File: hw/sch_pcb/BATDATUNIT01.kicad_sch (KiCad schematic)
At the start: 115 parts, among them IC1 MAX14502AETL+, J1 USBC_USB4105-GF-A, J22 HEADER_2x03, J4 46436-9327, J9 SD_Card-FPS009-4200-0, Q1 BC817-25, Q2 BC817-25, Q3 BC817-25, Q4 BC817-25, SW3 KMT031, SW3 SKRTLAE010, SW4 KMT031, SW4 SKRTLAE010, U10 ATMEGA1284P-AU, U11 PCF85263A, U11 TCA4307, U2 USBLC6-2SC6, U3 FT260Q-T, U4 PCA9541ABS/01, U6 AT24CS64-SSHM, U6 SHT35-DIS, U7 TMUX1574DYYR, Y1 19.2 MHz, Y1 8 MHz, Y2 ABS07-120-32.768KHZ-T

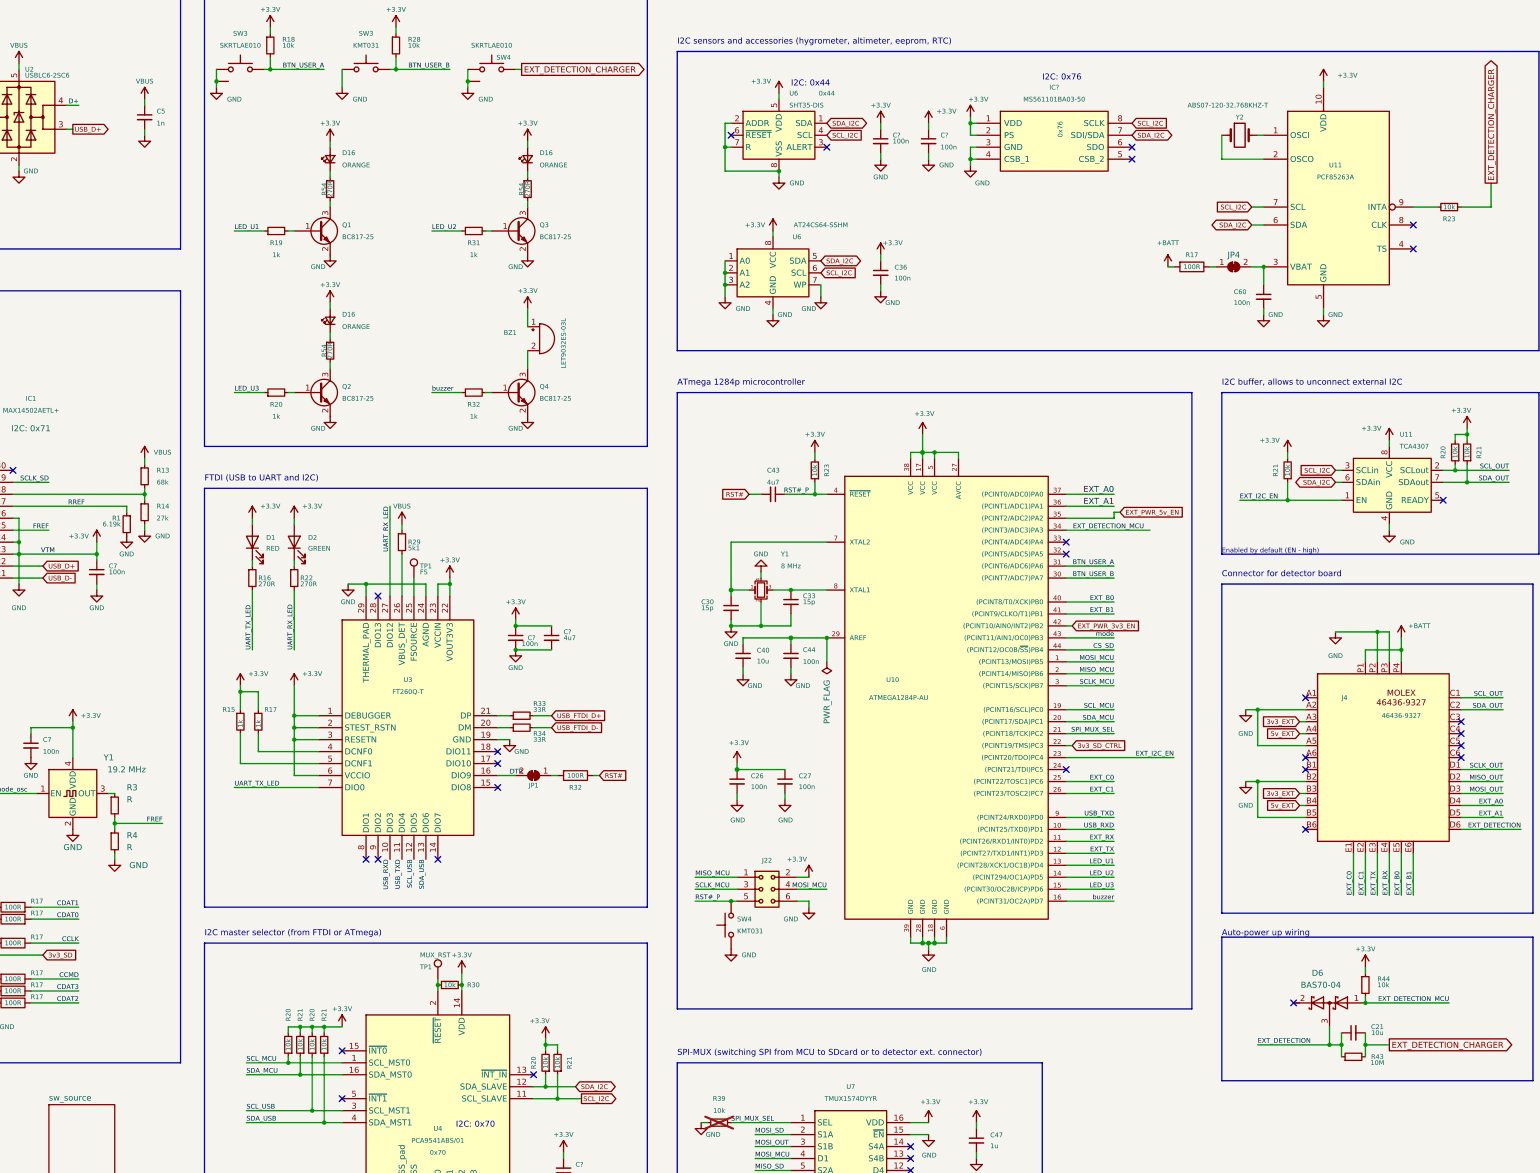
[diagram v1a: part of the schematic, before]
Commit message: Add power consumption notes to schematics.
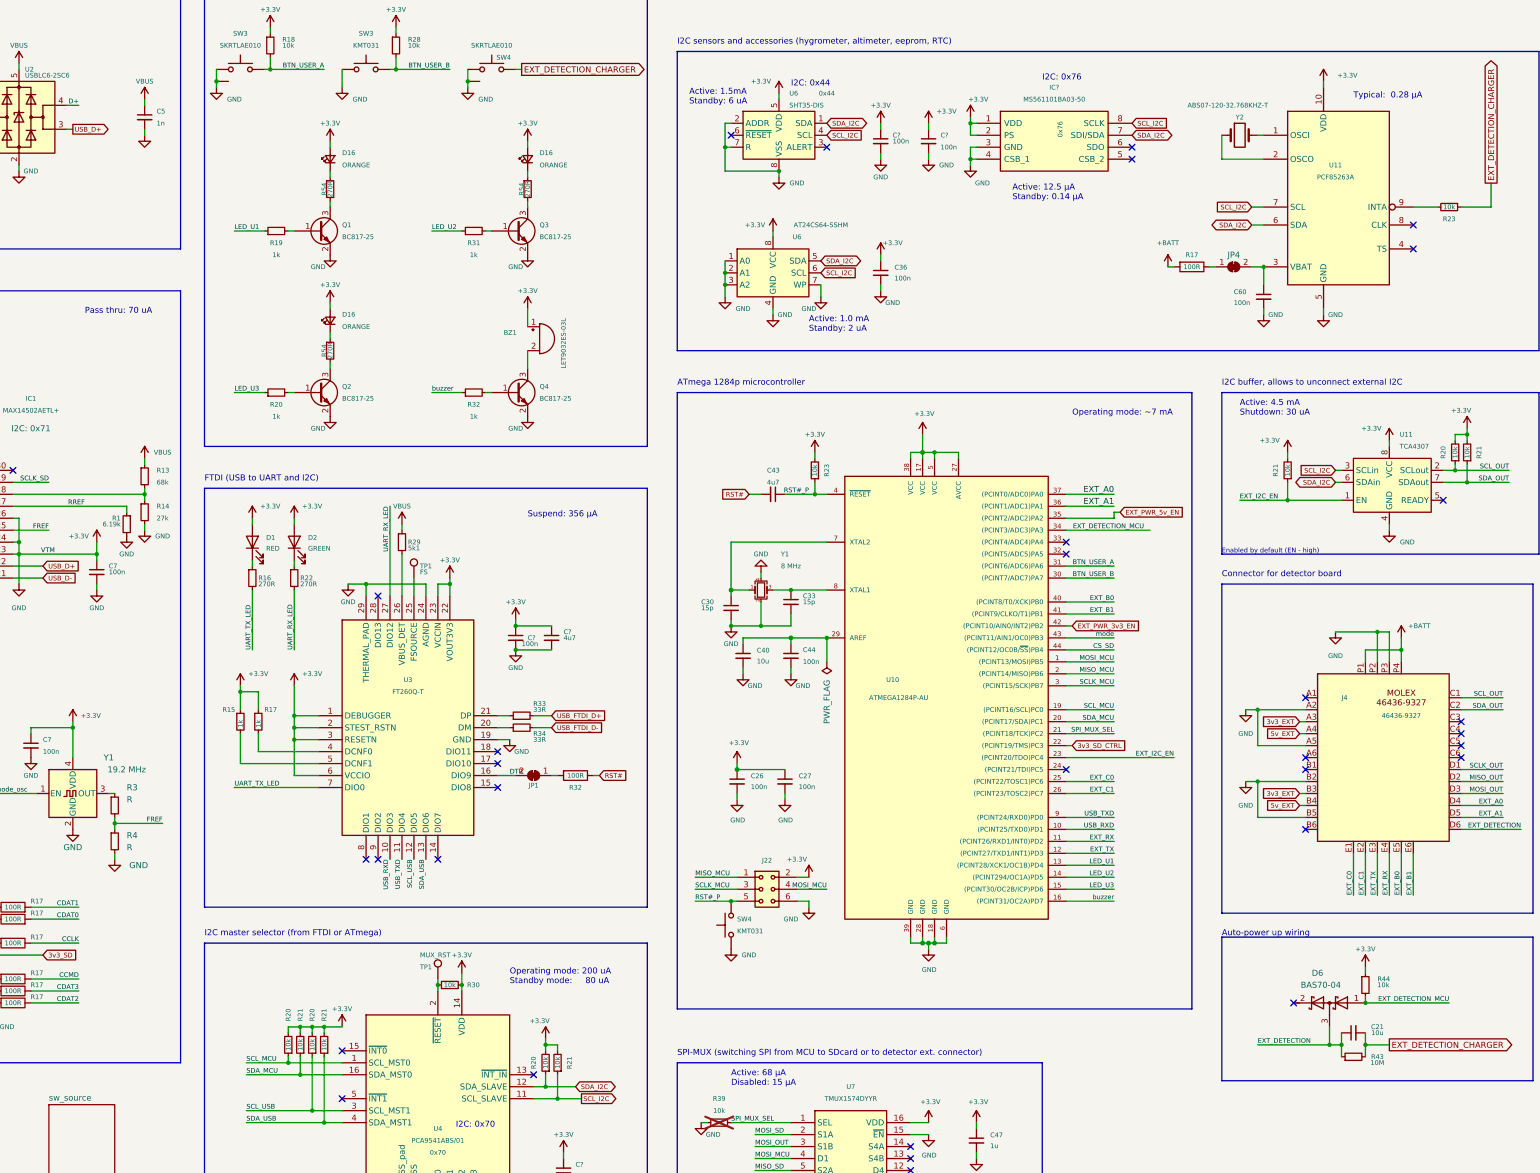
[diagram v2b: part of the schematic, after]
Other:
- note added: "Active: 1.0 mA Standby: 2 uA"
- note added: "Active: 1.5mA Standby: 6 uA"
- note added: "Active: 12.5 μA Standby: 0.14 μA"
- note added: "Active: 4.5 mA Shutdown: 30 uA"
- note added: "Active: 68 μA Disabled: 15 μA"
- note added: "Operating mode: 200 uA Standby mode: 80 uA"
- note added: "Operating mode: ~7 mA"
- note added: "Pass thru: 70 uA"
- note added: "Suspend: 356 μA"
- note added: "Typical: 0.28 μA"
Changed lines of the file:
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@@
     (effects (font (size 1.27 1.27)) (justify left bottom))
   )
+  (text "Active: 4.5 mA\nShutdown: 30 uA" (at 341.63 109.22 0)
+    (effects (font (size 1.27 1.27)) (justify left bottom))
+  )
+  (text "Active: 1.5mA\nStandby: 6 uA" (at 224.79 43.18 0)
+    (effects (font (size 1.27 1.27)) (justify left bottom))
+  )
+  (text "Active: 1.0 mA\nStandby: 2 uA" (at 250.19 91.44 0)
+    (effects (font (size 1.27 1.27)) (justify left bottom))
+  )
+  (text "Suspend: 356 μA" (at 190.5 130.81 0)
+    (effects (font (size 1.27 1.27)) (justify left bottom))
+  )
   (text "FTDI (USB to UART and I2C)" (at 121.92 123.19 0)
     (effects (font (size 1.27 1.27)) (justify left bottom))
@@
     (effects (font (size 1.27 1.27)) (justify left bottom))
   )
+  (text "Active: 12.5 μA\nStandby: 0.14 μA" (at 293.37 63.5 0)
+    (effects (font (size 1.27 1.27)) (justify left bottom))
+  )
   (text "Mechanical" (at 15.24 250.19 0)
     (effects (font (size 1.27 1.27)) (justify left bottom))
@@
     (effects (font (size 1.27 1.27)) (justify left bottom))
   )
+  (text "Pass thru: 70 uA" (at 96.52 87.63 0)
+    (effects (font (size 1.27 1.27)) (justify left bottom))
+  )
   (text "USB-C connector and ESD protection" (at 15.24 19.05 0)
     (effects (font (size 1.27 1.27)) (justify left bottom))
   )
+  (text "Typical:  0.28 μA " (at 365.76 41.91 0)
+    (effects (font (size 1.27 1.27)) (justify left bottom))
+  )
   (text "I2C sensors and accessories (hygrometer, altimeter, eeprom, RTC)"
     (at 222.25 30.48 0)
@@
     (effects (font (size 1.27 1.27)) (justify left bottom))
   )
+  (text "Operating mode: ~7 mA" (at 306.07 109.22 0)
+    (effects (font (size 1.27 1.27)) (justify left bottom))
+  )
   (text "Auto-power up wiring" (at 337.82 219.71 0)
     (effects (font (size 1.27 1.27)) (justify left bottom))
   )
+  (text "Active: 68 μA\nDisabled: 15 μA" (at 233.68 251.46 0)
+    (effects (font (size 1.27 1.27)) (justify left bottom))
+  )
   (text "Connector for detector board" (at 337.82 143.51 0)
     (effects (font (size 1.27 1.27)) (justify left bottom))
@@
     (effects (font (size 1.27 1.27)) (justify left bottom))
   )
+  (text "Operating mode: 200 uA\nStandby mode: 	80 uA" (at 186.69 229.87 0)
+    (effects (font (size 1.27 1.27)) (justify left bottom))
+  )
   (text "SD card interface (USB to SDcard reader and USB-bridge to FTDI)"
     (at 15.24 81.28 0)
@@
       (effects (font (size 1 1)) (justify left) hide)
     )
-    (property "Datasheet" "http://www.te.com/usa-en/search.html?q=ms5611&source=header" (at 314.96 46.99 0)
+    (property "Datasheet" "https://www.te.com/usa-en/product-MS561101BA03-50.datasheet.pdf" (at 314.96 46.99 0)
       (effects (font (size 1 1)) (justify left) hide)
     )

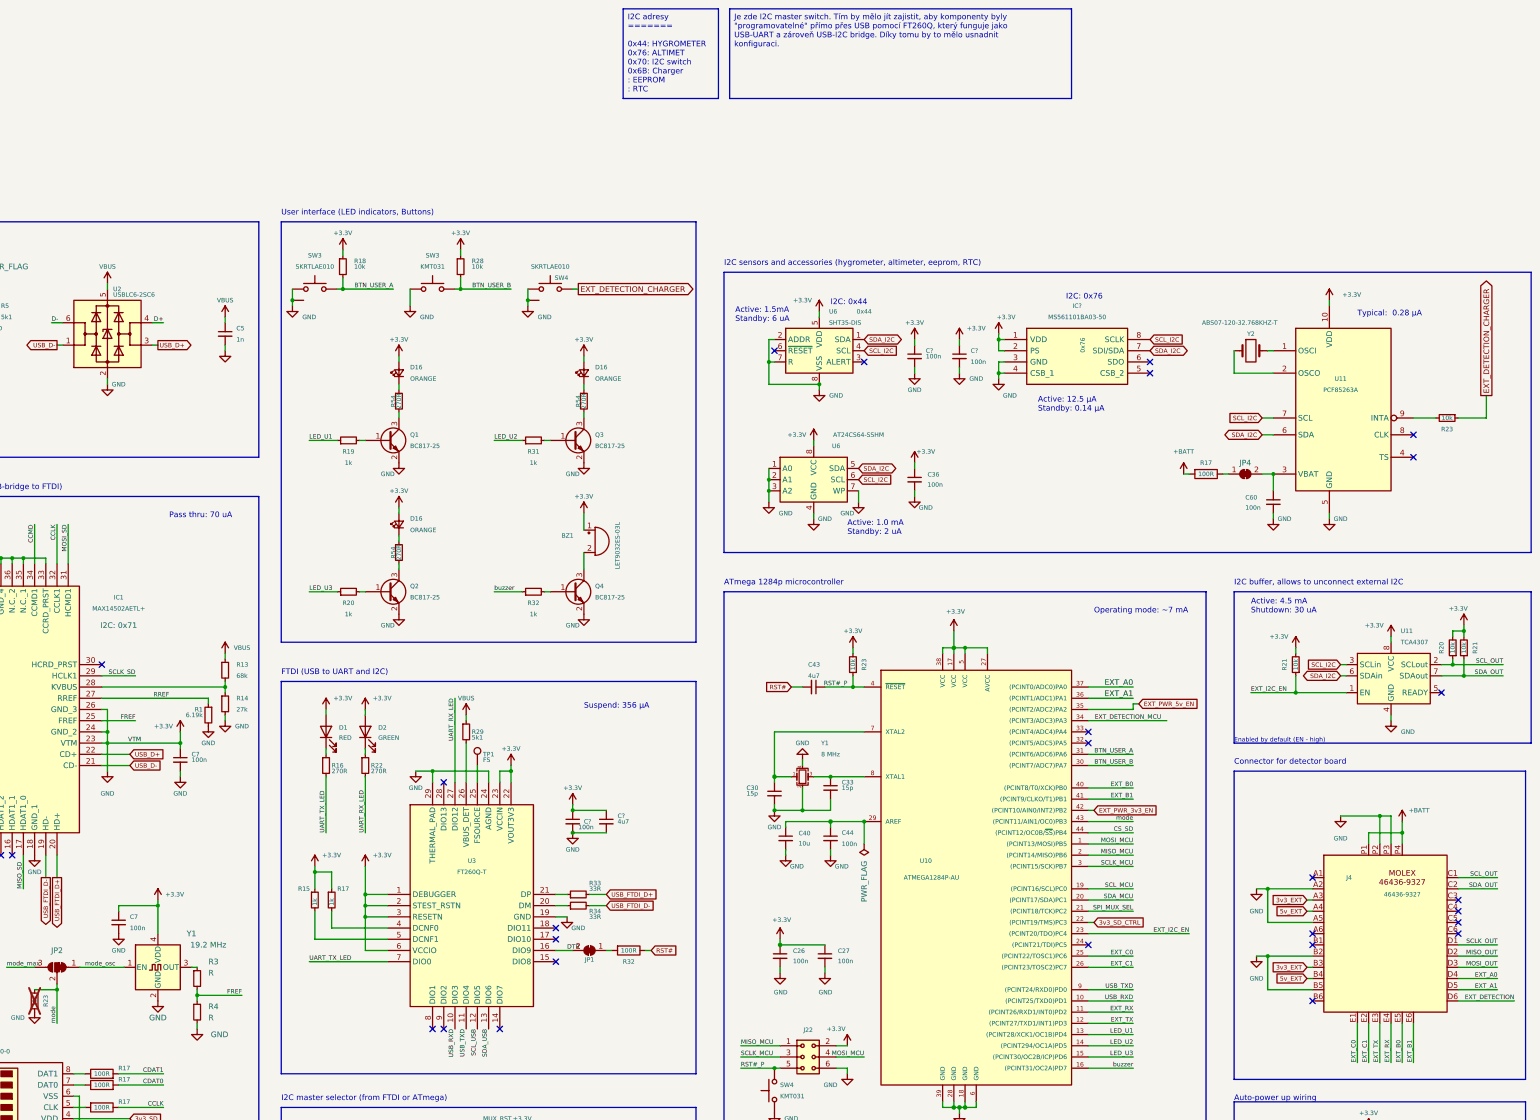
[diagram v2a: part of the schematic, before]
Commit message: Vylepseni, upravy layoutu, zmena ovladani ledky, reset pin do molex konektoru
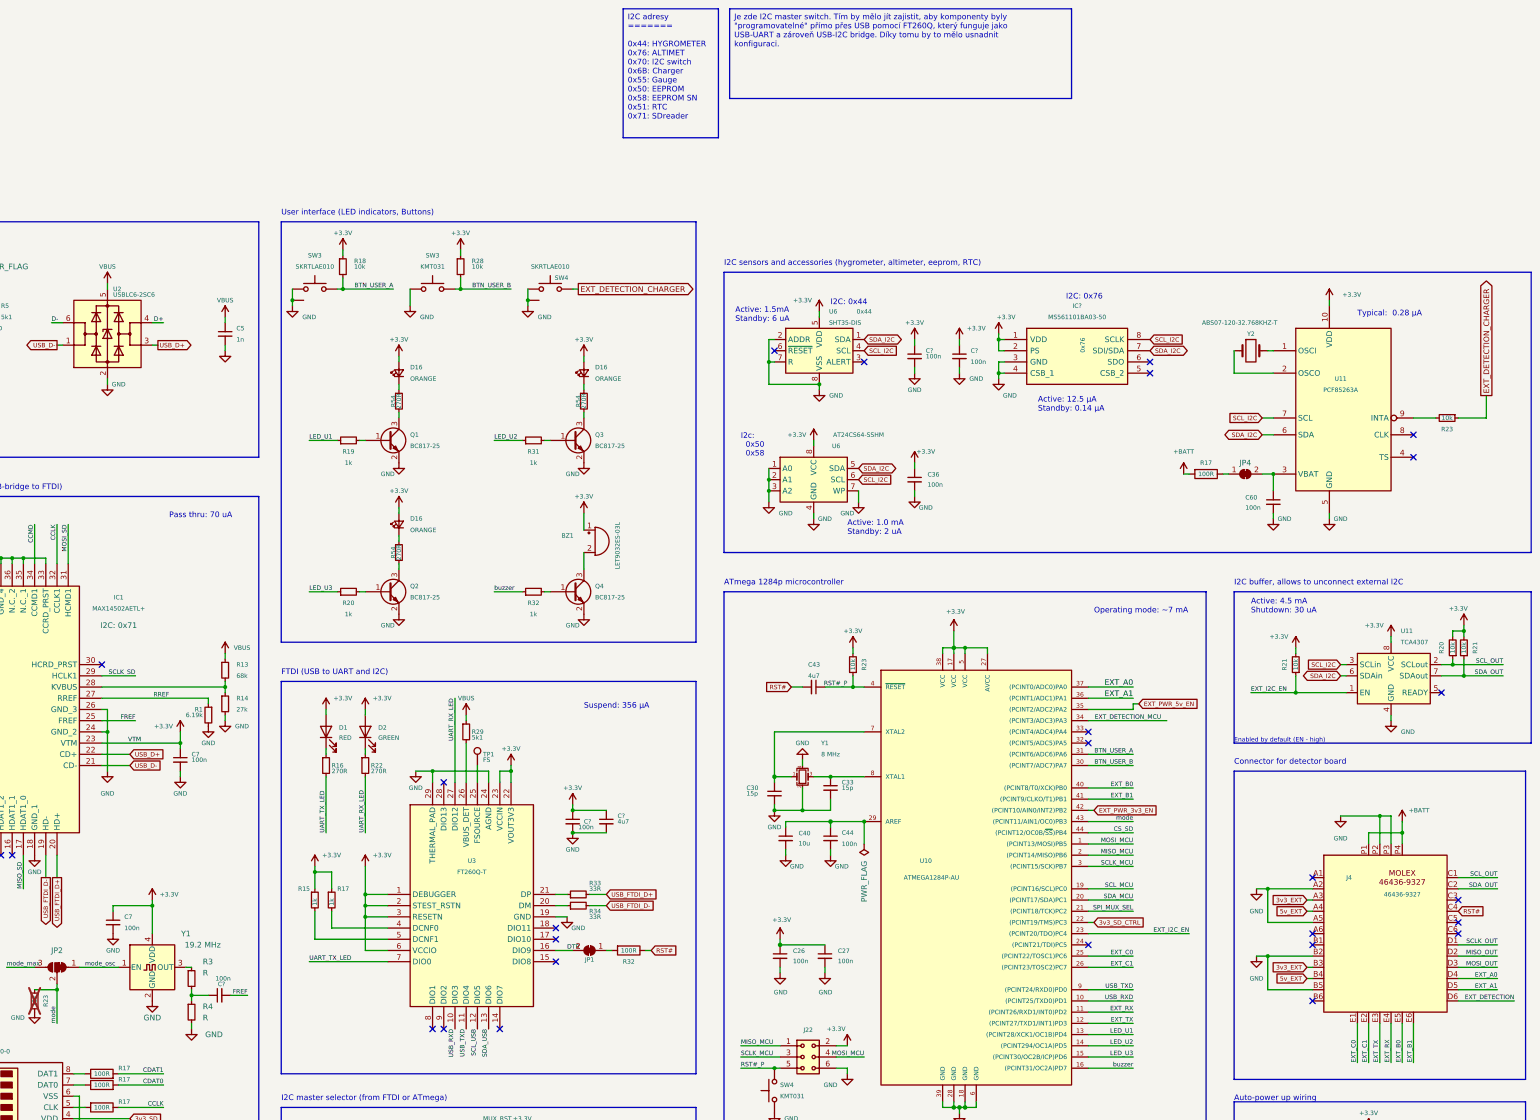
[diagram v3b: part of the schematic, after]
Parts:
- added C?: 100n, Capacitor_SMD:C_0805_2012Metric, symbol Device:C_Small
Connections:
- net +3.3V: no longer C26.2, C27.2, C30.2, C33.2, C36.2, C40.2, C44.2, C47.2, C5.2, C5.2, C6.2, C60.2, C7.2, C7.2, C?.2, C?.2, C?.2, C?.2, C?.2, H1.1, H2.1, H3.1, H4.1, IC1.18 (GND_1), IC1.24 (GND_2), IC1.26 (GND_3), IC1.33 (CCRD_PRST), IC1.35 (N.C._1), IC1.36 (N.C._2), IC1.37 (GND_4), IC1.41 (GND_5), IC?.3 (GND), IC?.4 (CSB_1), J1.A1/B12 (GND), J1.B1/A12 (GND), J1.G1 (SHIELD), J1.G2 (SHIELD), J1.G3 (SHIELD), J1.G4 (SHIELD), J22.6, J4.A2, J4.A5, J4.B2, J4.B5, J4.P2, J4.P3, J9.12 (SHELL1), J9.3 (VSS), J9.6 (VSS), JP1.3 (B), Q1.2 (E), Q2.2 (E), Q3.2 (E), Q4.2 (E), R1.2, R14.2, R2.1, R23.1, R39.1, R4.2, R5.1, SW3.2, SW3.2, SW3.GND (SHIELD), SW4.1, SW4.2, SW4.GND (SHIELD), U10.18 (GND), U10.28 (GND), U10.39 (GND), U10.6 (GND), U11.4 (GND), U11.5 (GND), U2.2 (GND), U3.19 (GND), U3.24 (AGND), U3.29 (THERMAL_PAD), U4.10 (A3), U4.17 (VSS_pad), U4.6 (VSS), U4.7 (A0), U4.8 (A1), U4.9 (A2), U6.1 (A0), U6.2 (A1), U6.2 (ADDR), U6.3 (A2), U6.4 (GND), U6.7 (R), U6.7 (WP), U6.8 (VSS), U6.9 (VSS), U7.15 (~{EN}), U7.8 (GND), Y1.2, Y1.2 (GND), Y1.4
- net FREF: now also C?.2; no longer R3.2, R4.1
- net RST#: now also J4.C4
- new net: C?.1, R3.2, R4.1
- new net GND: C26.2, C27.2, C30.2, C33.2, C36.2, C40.2, C44.2, C47.2, C5.2, C5.2, C6.2, C60.2, C7.2, C7.2, C?.2, C?.2, C?.2, C?.2, C?.2, H1.1, H2.1, H3.1, H4.1, IC1.18 (GND_1), IC1.24 (GND_2), IC1.26 (GND_3), IC1.33 (CCRD_PRST), IC1.35 (N.C._1), IC1.36 (N.C._2), IC1.37 (GND_4), IC1.41 (GND_5), IC?.3 (GND), IC?.4 (CSB_1), J1.A1/B12 (GND), J1.B1/A12 (GND), J1.G1 (SHIELD), J1.G2 (SHIELD), J1.G3 (SHIELD), J1.G4 (SHIELD), J22.6, J4.A2, J4.A5, J4.B2, J4.B5, J4.P2, J4.P3, J9.12 (SHELL1), J9.3 (VSS), J9.6 (VSS), JP1.3 (B), Q1.2 (E), Q2.2 (E), Q3.2 (E), Q4.2 (E), R1.2, R14.2, R2.1, R23.1, R39.1, R4.2, R5.1, SW3.2, SW3.2, SW3.GND (SHIELD), SW4.1, SW4.2, SW4.GND (SHIELD), U10.18 (GND), U10.28 (GND), U10.39 (GND), U10.6 (GND), U11.4 (GND), U11.5 (GND), U2.2 (GND), U3.19 (GND), U3.24 (AGND), U3.29 (THERMAL_PAD), U4.10 (A3), U4.17 (VSS_pad), U4.6 (VSS), U4.7 (A0), U4.8 (A1), U4.9 (A2), U6.1 (A0), U6.2 (A1), U6.2 (ADDR), U6.3 (A2), U6.4 (GND), U6.7 (R), U6.7 (WP), U6.8 (VSS), U6.9 (VSS), U7.15 (~{EN}), U7.8 (GND), Y1.2, Y1.2 (GND), Y1.4
- no-connect marks 39 -> 38
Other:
- note added: "I2c: 0x50 0x58"
- moved on the sheet: C7, R3, R4, Y1
